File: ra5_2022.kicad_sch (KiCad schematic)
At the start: 0 parts

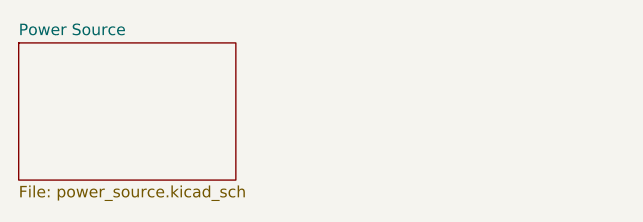
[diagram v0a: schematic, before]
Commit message: Add MCU and M90E32AS sheets, import connector/switch/MCU parts
Adds the mcu.kicad_sch and m90e32as.kicad_sch hierarchical sheets and
wires them into the root schematic and PCB. Imports several LCSC parts
into the project-local ra5_2022 library (symbols/footprints/3D models):
USB-C connectors, TQFP-48 MCU footprint, tactile switch, and the
DB126V-5.0-2P terminal block, plus adds schematic-only symbols for the
MX15EDGRHC-3.5-2x03P receptacle and its MX15EDGKNH-3.5-2x03P mating
plug (BOM-only, not placed on board). Checks in CLAUDE.md.
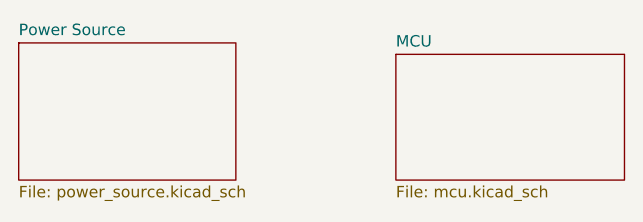
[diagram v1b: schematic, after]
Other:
- added sheet MCU (mcu.kicad_sch)
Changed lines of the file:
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@@
+		)
+	)
+	(sheet
+		(at 92.71 49.53)
+		(size 25.4 13.97)
+		(exclude_from_sim no)
+		(in_bom yes)
+		(on_board yes)
+		(dnp no)
+		(fields_autoplaced yes)
+		(stroke
+			(width 0.1524)
+			(type solid)
+		)
+		(fill
+			(color 0 0 0 0)
+		)
+		(property "Sheetname" "MCU"
+			(at 92.71 48.8184 0)
+			(show_name no)
+			(do_not_autoplace no)
+			(effects
+				(font
+					(size 1.27 1.27)
+				)
+				(justify left bottom)
+			)
+		)
+		(property "Sheetfile" "mcu.kicad_sch"
+			(at 92.71 64.0846 0)
+			(show_name no)
+			(do_not_autoplace no)
+			(effects
+				(font
+					(size 1.27 1.27)
+				)
+				(justify left top)
+			)
+		)
+		(instances
+			(project "ra5_2022"
+				(path "/5cbb1e83-2d68-46fe-9857-942ec50591ae"
+					(page "3")
+				)
+			)
 		)
 	)
